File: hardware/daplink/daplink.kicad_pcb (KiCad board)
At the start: 2 copper layers, 50 x 20 mm, 33 parts, among them J1 Conn_01x04, J2 Conn_01x05, J3 Conn_01x05, P1 USB_C_Plug_USB2.0, U1 AMS1117-3.3, U2 STM32F103CBTx, Y1 8MHz

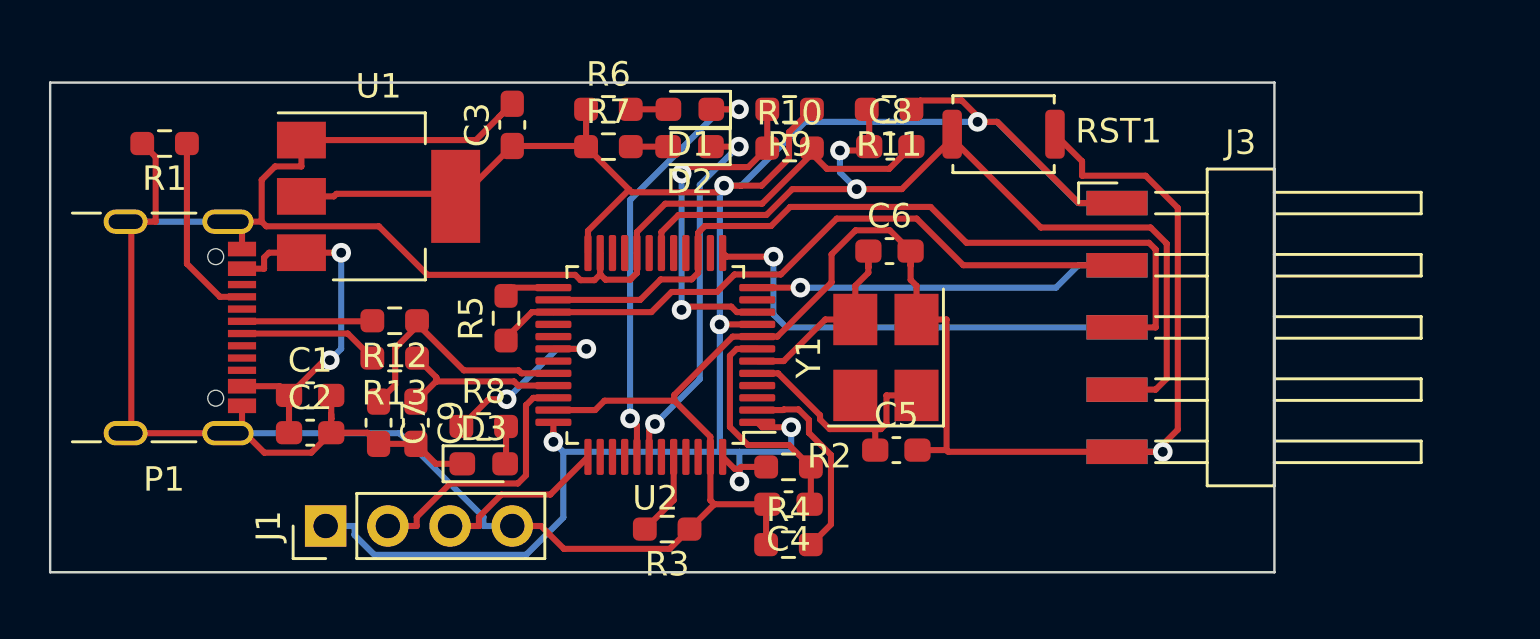
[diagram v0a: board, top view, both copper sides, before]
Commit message: feat(hw/schematic): refine placement
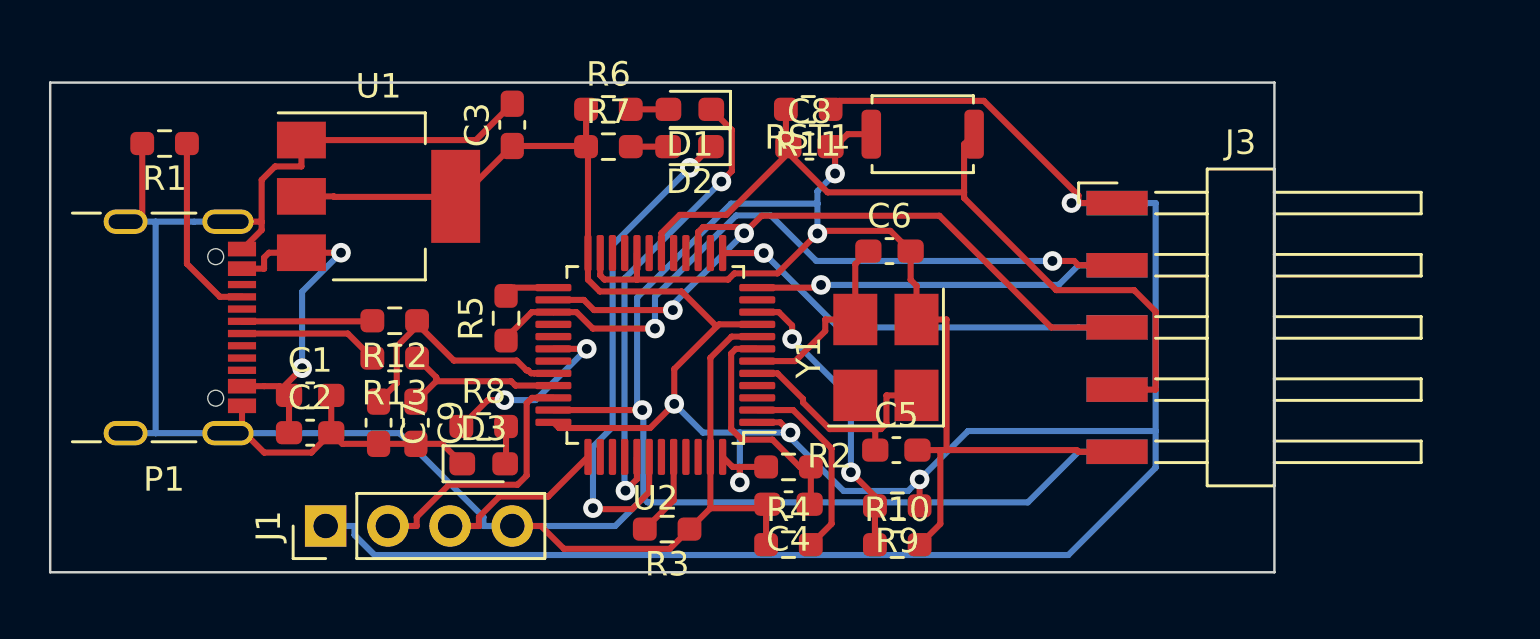
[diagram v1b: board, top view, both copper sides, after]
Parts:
- moved R10 16.8 mm to (134.6, 118.9)
- moved R9 16.8 mm to (134.6, 117.3)
- moved C8 3.30 mm to (131.0, 102.6)
- moved R11 3.30 mm to (131.0, 101.1)
- moved RST1 3.30 mm to (135.6, 102.1), turned to 180 degrees
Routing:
- net +3.3V: track 101.5 -> 130.4 mm, vias 6 -> 5
- net /PB6: track 15.4 -> 20.8 mm
- net /TGT_RST: track 37.4 -> 34.3 mm, vias 2 -> 0
- net /TGT_SWCLK: track 32.6 -> 29.7 mm, vias 0 -> 2
- net /PA0: track 14.3 -> 12.0 mm
- net GND: track 174.7 -> 176.4 mm, vias 1 -> 3
- net /PB5: track 17.7 -> 19.3 mm
- net /TGT_TX: track 18.8 -> 17.4 mm
- net /TGT_SWDIO: track 27.9 -> 29.3 mm, vias 0 -> 2
- net +5V: track 15.4 -> 14.7 mm

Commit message: refactor(hw/schematic): refine routing
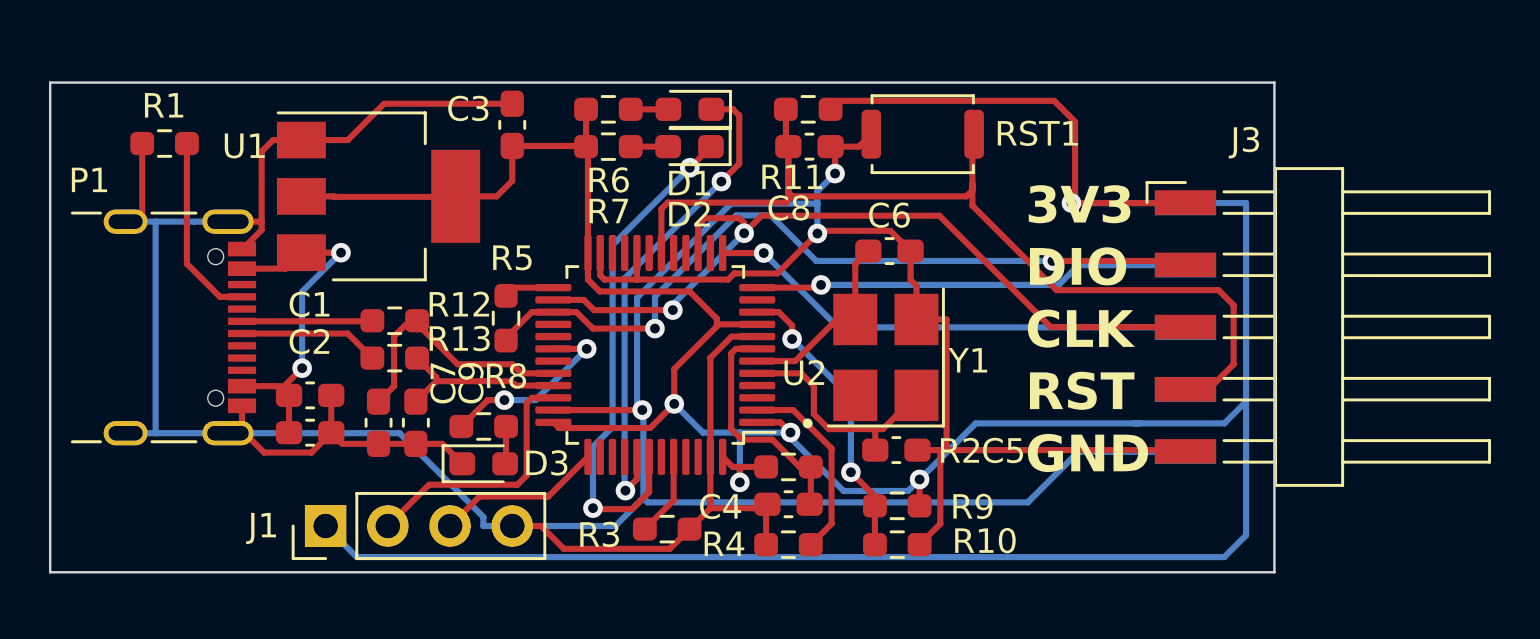
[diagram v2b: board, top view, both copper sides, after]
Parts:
- moved J3 2.79 mm to (151.9, 110.0)
- moved J2 2.79 mm to (151.9, 110.0)
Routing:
- net +3.3V: track 130.4 -> 149.2 mm
- net /TGT_RST: track 34.3 -> 40.6 mm
- net GND: track 176.4 -> 182.0 mm
- net /TGT_SWCLK: track 29.7 -> 33.2 mm
- net /TGT_TX: track 17.4 -> 20.2 mm
- net /TGT_RX: track 15.1 -> 17.9 mm
- net /TGT_SWDIO: track 29.3 -> 32.1 mm
- net /PB5: track 19.3 -> 20.1 mm
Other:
- board text added: "3V3"
- board text added: "CLK"
- board text added: "DIO"
- board text added: "GND"
- board text added: "RST"
- board text added: "RX"
- board text added: "TX"

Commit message: feat(hw/schematic): change the footprint of crystal
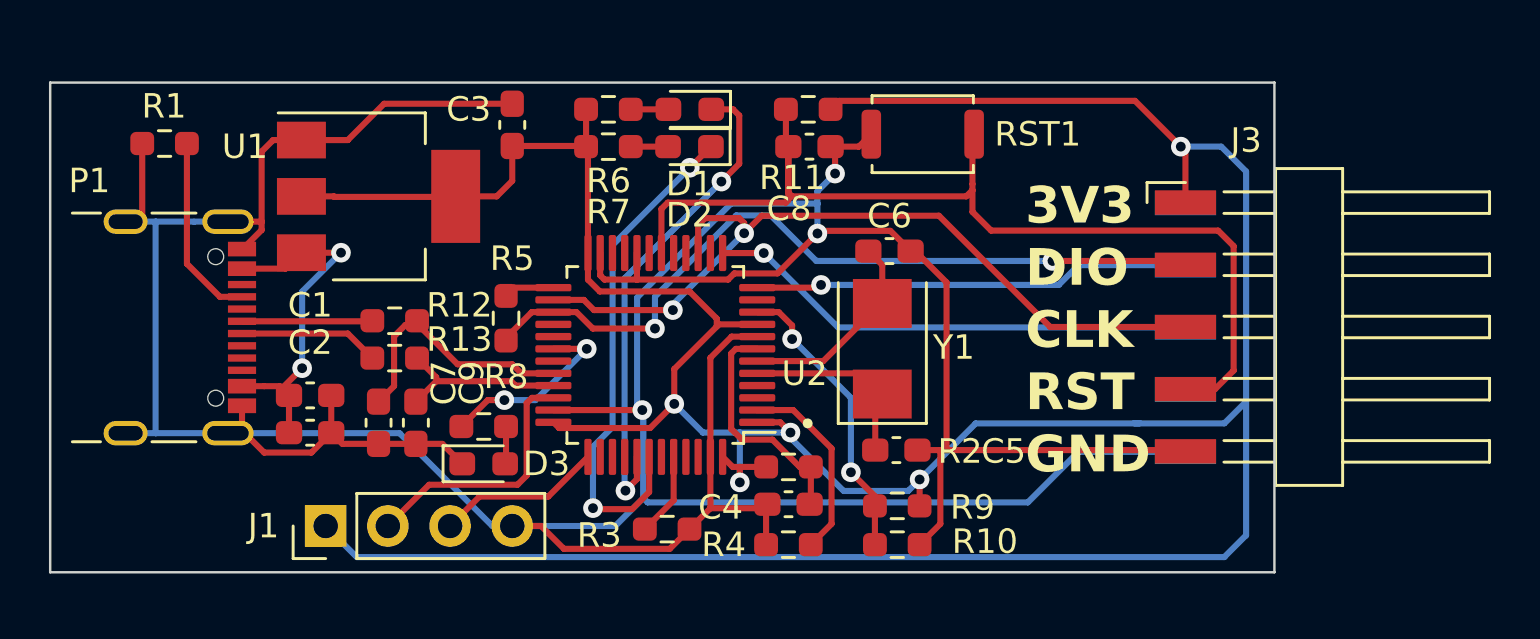
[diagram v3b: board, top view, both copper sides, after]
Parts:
- C5, C6: value 10nF -> 8pF
- D1: value LED -> LEDB
- D2: value LED -> LEDG
- D3: value LED -> LEDR
- Y1: footprint Crystal:Crystal_SMD_SeikoEpson_FA238V-4Pin_3.2x2.5mm_HandSoldering -> Crystal:Crystal_SMD_5032-2Pin_5.0x3.2mm
- moved Y1 0.38 mm to (134.0, 110.9)
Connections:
- Y1 pad 2: GND -> /OSCOUT
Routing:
- net +3.3V: track 149.2 -> 145.6 mm
- net /OSCIN: track 9.55 -> 7.87 mm
- net /TGT_RST: track 40.6 -> 42.0 mm
- net GND: track 182.0 -> 181.2 mm
- net /OSCOUT: track 7.72 -> 8.46 mm

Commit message: feat(hw/pcb): signed
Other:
- board text added: "By Andy.C"
- board text added: "DAPLink v1"
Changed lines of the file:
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@@
     (property "ki_keywords" "connector")
     (attr through_hole)
-    (fp_text reference "J1" (at 0 -2.54 180) (layer "F.SilkS")
+    (fp_text reference "J1" (at 2.413 -0.127 180) (layer "F.SilkS")
         (effects (font (size 1 1) (thickness 0.15)))
     )
@@
     (effects (font (size 1.5 1.5) (thickness 0.3) bold) (justify left bottom mirror))
   )
+  (gr_text "By Andy.C" (at 121.285 105.41) (layer "B.SilkS")
+    (effects (font (size 1.5 1.5) (thickness 0.3) bold) (justify left bottom mirror))
+  )
   (gr_text "CLK" (at 139.827 110.98) (layer "F.SilkS")
     (effects (font (size 1.5 1.5) (thickness 0.3) bold) (justify left bottom))
   )
+  (gr_text "DAPLink\nv1" (at 100.076 119.888) (layer "F.SilkS")
+    (effects (font (size 1.5 1.5) (thickness 0.3) bold) (justify left bottom))
+  )

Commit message: fix(hw/layout): refine rounting
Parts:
- C5, C6: value 8pF -> 20pF
- moved R5 3.36 mm to (119.7, 106.4), turned to 0 degrees
- moved R13 1.77 mm to (113.4, 109.6)
- moved R12 1.53 mm to (113.4, 111.1)
- moved C7 1.52 mm to (114.9, 113.9)
- moved C9 1.52 mm to (113.4, 113.9)
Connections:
- J2 pad 3: /TGT_TX -> /TGT_RX
- J2 pad 4: /TGT_RX -> /TGT_TX
- R12 pad 2: /D+ -> /D-
- R13 pad 2: /D- -> /D+
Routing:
- net +3.3V: track 145.6 -> 117.9 mm, vias 5 -> 7
- net GND: track 181.2 -> 187.2 mm, vias 3 -> 4
- net /PA12: track 7.31 -> 12.8 mm, vias 0 -> 2
- net /PA11: track 10.6 -> 8.66 mm
- net /TGT_SWDIO: track 32.1 -> 34.0 mm
- net /D-: track 5.74 -> 5.05 mm
- net /D+: track 5.33 -> 4.75 mm

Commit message: fix(hw/sch): fix led and R5
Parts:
- D1: value LEDB -> LEDG
- D2: value LEDG -> LEDB
- R5: value 4K7 -> 100
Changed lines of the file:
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@@
         (effects (font (size 1 1) (thickness 0.15)))
     )
-    (fp_text value "4K7" (at 0.127 1.427) (layer "F.Fab")
+    (fp_text value "100" (at 0.127 1.427) (layer "F.Fab")
         (effects (font (size 1 1) (thickness 0.15)))
     )
@@
         (effects (font (size 1 1) (thickness 0.15)))
     )
-    (fp_text value "LEDG" (at 0 1.43) (layer "F.Fab")
+    (fp_text value "LEDB" (at 0 1.43) (layer "F.Fab")
         (effects (font (size 1 1) (thickness 0.15)))
     )
@@
         (effects (font (size 1 1) (thickness 0.15)))
     )
-    (fp_text value "LEDB" (at 0 1.43) (layer "F.Fab")
-        (effects (font (size 1 1) (thickness 0.15)))
-    )
+    (fp_text value "LEDG" (at 0 1.43) (layer "F.Fab")
+        (effects (font (size 1 1) (thickness 0.15)))
+    )

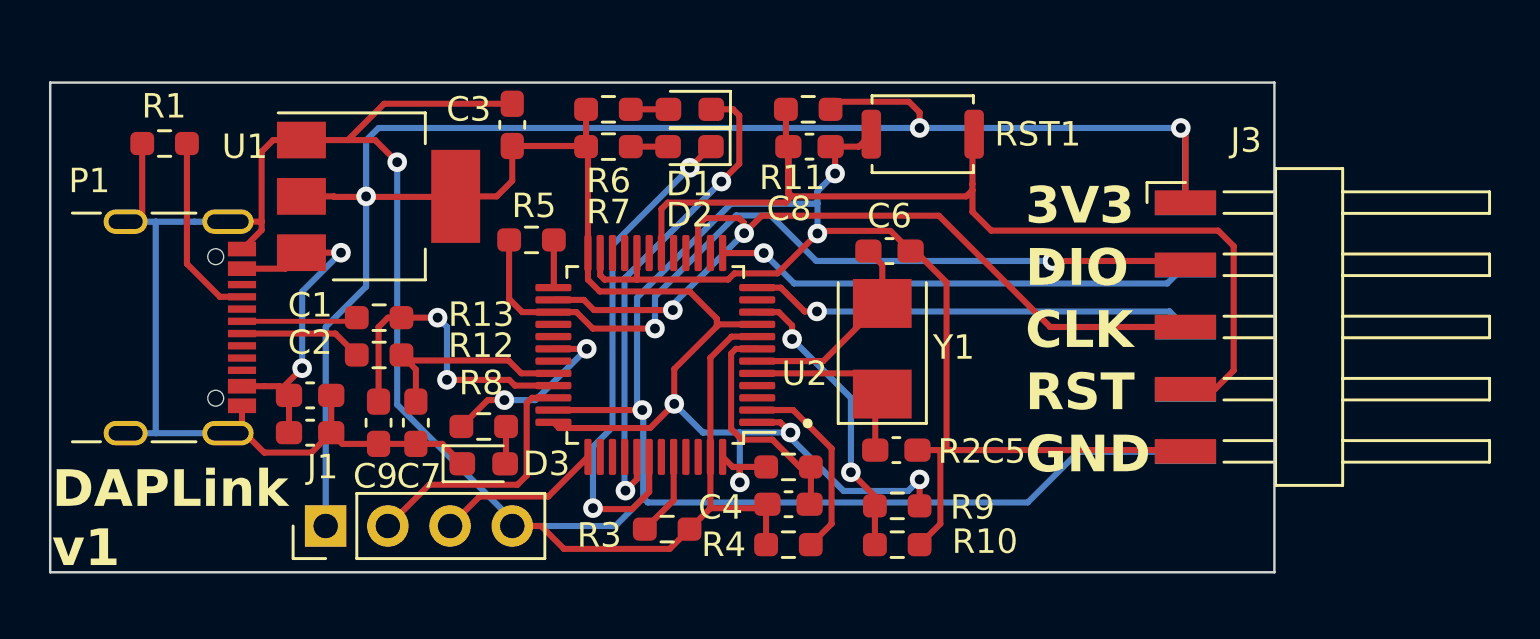
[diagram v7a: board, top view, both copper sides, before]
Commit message: fix(hw/usb): d+ pull up and support usb-c flip
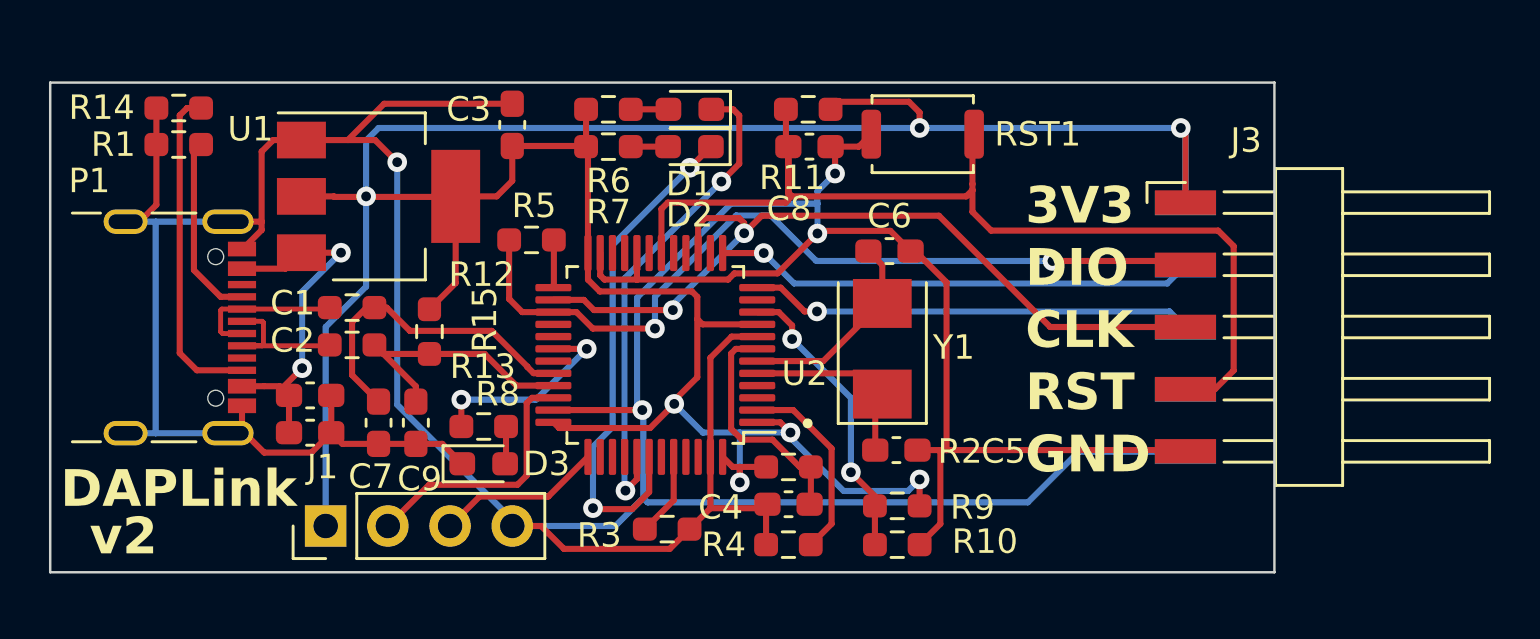
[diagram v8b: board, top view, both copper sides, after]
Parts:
- added R14: 5K1, Resistor_SMD:R_0603_1608Metric_Pad0.98x0.95mm_HandSolder, F.Cu at (105.2, 101.0)
- added R15: 1K5, Resistor_SMD:R_0603_1608Metric_Pad0.98x0.95mm_HandSolder, F.Cu at (115.5, 110.2)
- P1: value USB_C_Plug_USB2.0 -> USB_C_Receptacle_USB2.0
- R1: value 10K -> 5K1
- moved R12 2.23 mm to (112.3, 109.2)
- moved R13 1.57 mm to (112.3, 110.7)
- moved C7 1.52 mm to (113.4, 113.9)
- moved C9 1.52 mm to (114.9, 113.9)
- moved R1 0.58 mm to (105.2, 102.5)
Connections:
- P1 pad A8: (no net) -> unconnected-(P1-SBU1-PadA8)
- P1 pad B5: unconnected-(P1-VCONN-PadB5) -> Net-(P1-CC2)
- P1 pad B6: (no net) -> /D+
- P1 pad B7: (no net) -> /D-
- P1 pad B8: (no net) -> unconnected-(P1-SBU2-PadB8)
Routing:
- net Net-(P1-CC2): track 0.00 -> 13.5 mm
- net +3.3V: track 117.9 -> 123.2 mm
- net /PA11: track 8.66 -> 13.3 mm
- net /PA12: track 12.8 -> 11.0 mm, vias 2 -> 0
- net GND: track 187.2 -> 188.9 mm
- net /D+: track 4.75 -> 6.29 mm
- net /D-: track 5.05 -> 6.28 mm
- net /PA9: track 7.80 -> 8.44 mm
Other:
- board text added: "DAPLink"
- board text added: "v2"
- board text removed: "DAPLink v1"
